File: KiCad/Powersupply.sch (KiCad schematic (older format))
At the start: 12 parts, among them J501 TE_Connectivity_282834-3, J502 CONN_01X03_FEMALE, U501 LM1086-5V, U502 LM1086-3.3V

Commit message: Updated a few components and links
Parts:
- D501: value MBR340 -> MBRS360BT3G
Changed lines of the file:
@@
 P 1500 2950
 F 0 "D501" H 1500 2734 50  0000 C CNN
-F 1 "MBR340" H 1500 2825 50  0000 C CNN
+F 1 "MBRS360BT3G" H 1500 2825 50  0000 C CNN
 F 2 "Diodes_SMD:D_SMB" H 1500 2775 50  0001 C CNN
-F 3 "" H 1500 2950 50  0001 C CNN
+F 3 "https://www.digikey.se/product-detail/en/on-semiconductor/MBRS360BT3G/MBRS360BT3GOSCT-ND/2623453" H 1500 2950 50  0001 C CNN
 	1    1500 2950
 	-1   0    0    1

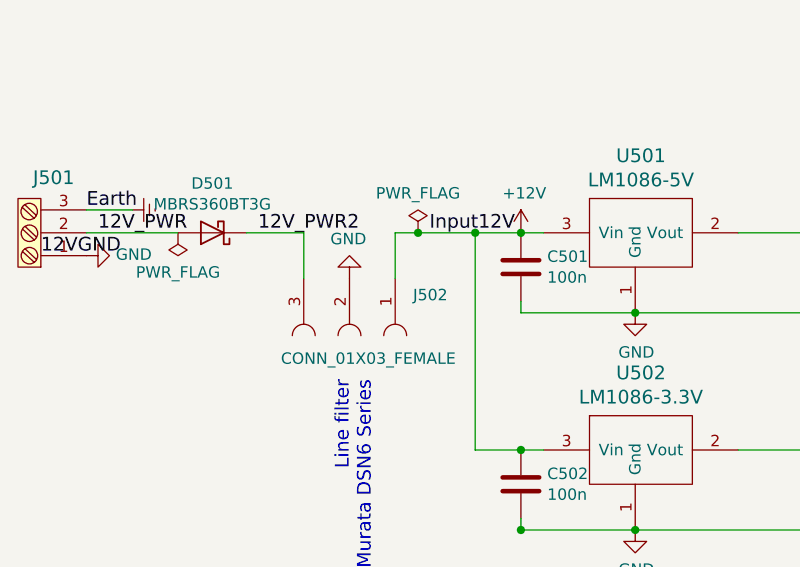
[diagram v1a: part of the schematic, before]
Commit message: Updated EMI component
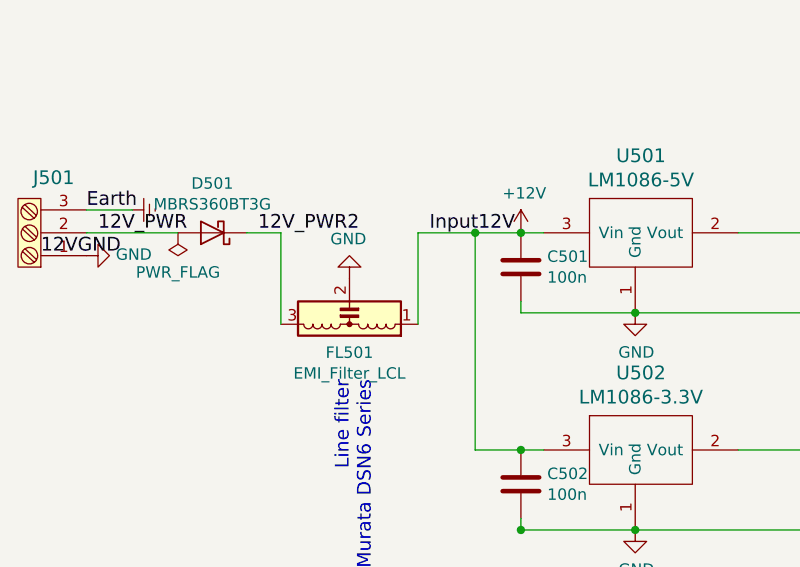
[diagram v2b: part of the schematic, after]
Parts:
- removed J502: CONN_01X03_FEMALE, Pin_Headers:Pin_Header_Straight_1x03_Pitch2.54mm, symbol CONN_01X03_FEMALE
- added FL501: EMI_Filter_LCL, Pin_Headers:Pin_Header_Straight_1x03_Pitch2.54mm, symbol EMI_Filter_LCL
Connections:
- net +12V: now also FL501.1
- net 12V_PWR2: now also FL501.3
- net Earth: now also FL501.2
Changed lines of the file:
@@
 POWER3V3
 $Comp
-L +3V3 #PWR504
+L +3V3 #PWR0120
 U 1 1 592AD7CB
 P 2200 1500
-F 0 "#PWR504" H 2200 1350 50  0001 C CNN
+F 0 "#PWR0120" H 2200 1350 50  0001 C CNN
 F 1 "+3V3" V 2215 1628 50  0000 L CNN
 F 2 "" H 2200 1500 50  0001 C CNN
@@
 	2100 1500 2200 1500
 $Comp
-L PWR_FLAG #FLG503
+L PWR_FLAG #FLG0121
 U 1 1 592B4E13
 P 2850 1450
-F 0 "#FLG503" H 2850 1525 50  0001 C CNN
+F 0 "#FLG0121" H 2850 1525 50  0001 C CNN
 F 1 "PWR_FLAG" H 2850 1624 50  0000 C CNN
 F 2 "" H 2850 1450 50  0001 C CNN
@@
 $EndComp
 $Comp
-L GND #PWR506
+L GND #PWR0122
 U 1 1 592B4E96
 P 2850 1450
-F 0 "#PWR506" H 2850 1200 50  0001 C CNN
+F 0 "#PWR0122" H 2850 1200 50  0001 C CNN
 F 1 "GND" H 2855 1277 50  0000 C CNN
 F 2 "" H 2850 1450 50  0001 C CNN
@@
 $EndComp
 $Comp
-L GND #PWR510
+L GND #PWR0123
 U 1 1 5924C039
 P 3350 4250
-F 0 "#PWR510" H 3350 4000 50  0001 C CNN
+F 0 "#PWR0123" H 3350 4000 50  0001 C CNN
 F 1 "GND" H 3355 4077 50  0000 C CNN
 F 2 "" H 3350 4250 50  0001 C CNN
@@
 Connection ~ 4200 2950
 $Comp
-L GND #PWR501
+L GND #PWR0124
 U 1 1 5924DE85
 P 950 3050
-F 0 "#PWR501" H 950 2800 50  0001 C CNN
+F 0 "#PWR0124" H 950 2800 50  0001 C CNN
 F 1 "GND" V 955 2922 50  0000 R CNN
 F 2 "" H 950 3050 50  0001 C CNN
@@
 $EndComp
 $Comp
-L PWR_FLAG #FLG501
+L PWR_FLAG #FLG0125
 U 1 1 5924DE8B
 P 1350 2950
-F 0 "#FLG501" H 1350 3025 50  0001 C CNN
+F 0 "#FLG0125" H 1350 3025 50  0001 C CNN
 F 1 "PWR_FLAG" H 1350 3123 50  0000 C CNN
 F 2 "" H 1350 2950 50  0001 C CNN
@@
 	2050 1850 2200 1850
 $Comp
-L +5V #PWR505
+L +5V #PWR0126
 U 1 1 5924EF19
 P 2200 1850
-F 0 "#PWR505" H 2200 1700 50  0001 C CNN
+F 0 "#PWR0126" H 2200 1700 50  0001 C CNN
 F 1 "+5V" V 2215 1978 50  0000 L CNN
 F 2 "" H 2200 1850 50  0001 C CNN
@@
 $EndComp
 $Comp
-L GND #PWR509
+L GND #PWR0127
 U 1 1 5924DE5E
 P 3350 3300
-F 0 "#PWR509" H 3350 3050 50  0001 C CNN
+F 0 "#PWR0127" H 3350 3050 50  0001 C CNN
 F 1 "GND" H 3355 3127 50  0000 C CNN
 F 2 "" H 3350 3300 50  0001 C CNN
@@
 	950  2950 1350 2950
 $Comp
-L CONN_01X03_FEMALE J502
-U 1 1 5929068A
-P 2100 3250
-F 0 "J502" V 2072 3528 50  0000 L CNN
-F 1 "CONN_01X03_FEMALE" V 2350 2950 50  0000 L CNN
-F 2 "Pin_Headers:Pin_Header_Straight_1x03_Pitch2.54mm" H 2100 3450 50  0001 C CNN
-F 3 "" H 2100 3450 50  0001 C CNN
-	1    2100 3250
-	0    1    1    0
-$EndComp
-$Comp
-L GND #PWR503
+L GND #PWR0128
 U 1 1 592909E6
 P 2100 3150
-F 0 "#PWR503" H 2100 2900 50  0001 C CNN
+F 0 "#PWR0128" H 2100 2900 50  0001 C CNN
 F 1 "GND" H 2105 2977 50  0000 C CNN
 F 2 "" H 2100 3150 50  0001 C CNN
@@
 $EndComp
 Wire Wire Line
-	1650 2950 1900 2950
-Wire Wire Line
-	1900 2950 1900 3150
-$Comp
-L +12V #PWR507
+	1650 2950 1800 2950
+Wire Wire Line
+	1800 2950 1800 3350
+$Comp
+L +12V #PWR0129
 U 1 1 592CA1C3
 P 2850 2950
-F 0 "#PWR507" H 2850 2800 50  0001 C CNN
+F 0 "#PWR0129" H 2850 2800 50  0001 C CNN
 F 1 "+12V" H 2865 3123 50  0000 C CNN
 F 2 "" H 2850 2950 50  0001 C CNN
@@
 	2850 4250 4650 4250
 Connection ~ 4200 4250
-$Comp
-L PWR_FLAG #FLG502
-U 1 1 592EF7D9
-P 2400 2950
-F 0 "#FLG502" H 2400 3025 50  0001 C CNN
-F 1 "PWR_FLAG" H 2400 3123 50  0000 C CNN
-F 2 "" H 2400 2950 50  0001 C CNN
-F 3 "" H 2400 2950 50  0001 C CNN
-	1    2400 2950
-	1    0    0    -1
-$EndComp
 Wire Wire Line
 	2650 3900 2950 3900
 Wire Wire Line
-	2300 2950 2950 2950
-Wire Wire Line
-	2300 2950 2300 3150
-Connection ~ 2400 2950
-$Comp
-L Earth #PWR502
+	2400 2950 2950 2950
+Wire Wire Line
+	2400 2950 2400 3350
+$Comp
+L Earth #PWR0130
 U 1 1 5933481E
 P 1150 2850
-F 0 "#PWR502" H 1150 2600 50  0001 C CNN
+F 0 "#PWR0130" H 1150 2600 50  0001 C CNN
 F 1 "Earth" H 1150 2700 50  0001 C CNN
 F 2 "" H 1150 2850 50  0001 C CNN
@@
 $EndComp
 $Comp
-L Earth #PWR508
+L Earth #PWR0131
 U 1 1 59344C28
 P 3150 1500
-F 0 "#PWR508" H 3150 1250 50  0001 C CNN
+F 0 "#PWR0131" H 3150 1250 50  0001 C CNN
 F 1 "Earth" H 3150 1350 50  0001 C CNN
 F 2 "" H 3150 1500 50  0001 C CNN
@@
 Wire Wire Line
 	3800 3900 5150 3900
+$Comp
+L EMI_Filter_LCL FL501
+U 1 1 5941C834
+P 2100 3250
+F 0 "FL501" H 2100 3474 50  0000 C CNN
+F 1 "EMI_Filter_LCL" H 2100 3565 50  0000 C CNN
+F 2 "Pin_Headers:Pin_Header_Straight_1x03_Pitch2.54mm" V 2100 3250 50  0001 C CNN
+F 3 "http://www.digikey.se/scripts/DkSearch/dksus.dll?Detail&itemSeq=230679104&uq=636330546617449401" V 2100 3250 50  0001 C CNN
+	1    2100 3250
+	-1   0    0    1
+$EndComp
 $EndSCHEMATC
